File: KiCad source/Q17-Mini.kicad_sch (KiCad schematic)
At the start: 81 parts, among them J1 INPUT, J2-1 SPK+, J2-2 SPK-, J3-1 V+, J3-2 GND, J3-3 V-, Q1 IRF610, Q10 KSA992, Q11 BS250P, Q12 BD139, Q13 IRF610, Q14 IRF9610, Q15 FQA46N15, Q16 FQA36P15, Q2 KSA992, Q3 KSC1845, Q4 IRF9610, Q5 FQP3P20, Q6 FQP3N30, Q7 KSC1845, Q8 ZVN4206AV, Q9 BS250P, U1 OPA1641

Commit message: Update Q17-Mini.kicad_sch
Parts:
- removed H1: MountingHole, MountingHole:MountingHole_3.2mm_M3_Pad_Via, symbol Mechanical:MountingHole
- R23: value 10K -> 10k
- renumbered R30 to R30R
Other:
- note added: "Q8 : 2N7000 (not TA) or ZVN4206AV"
- note removed: "Q8 : 2N7000 (Not TA) or ZVN4206AV"

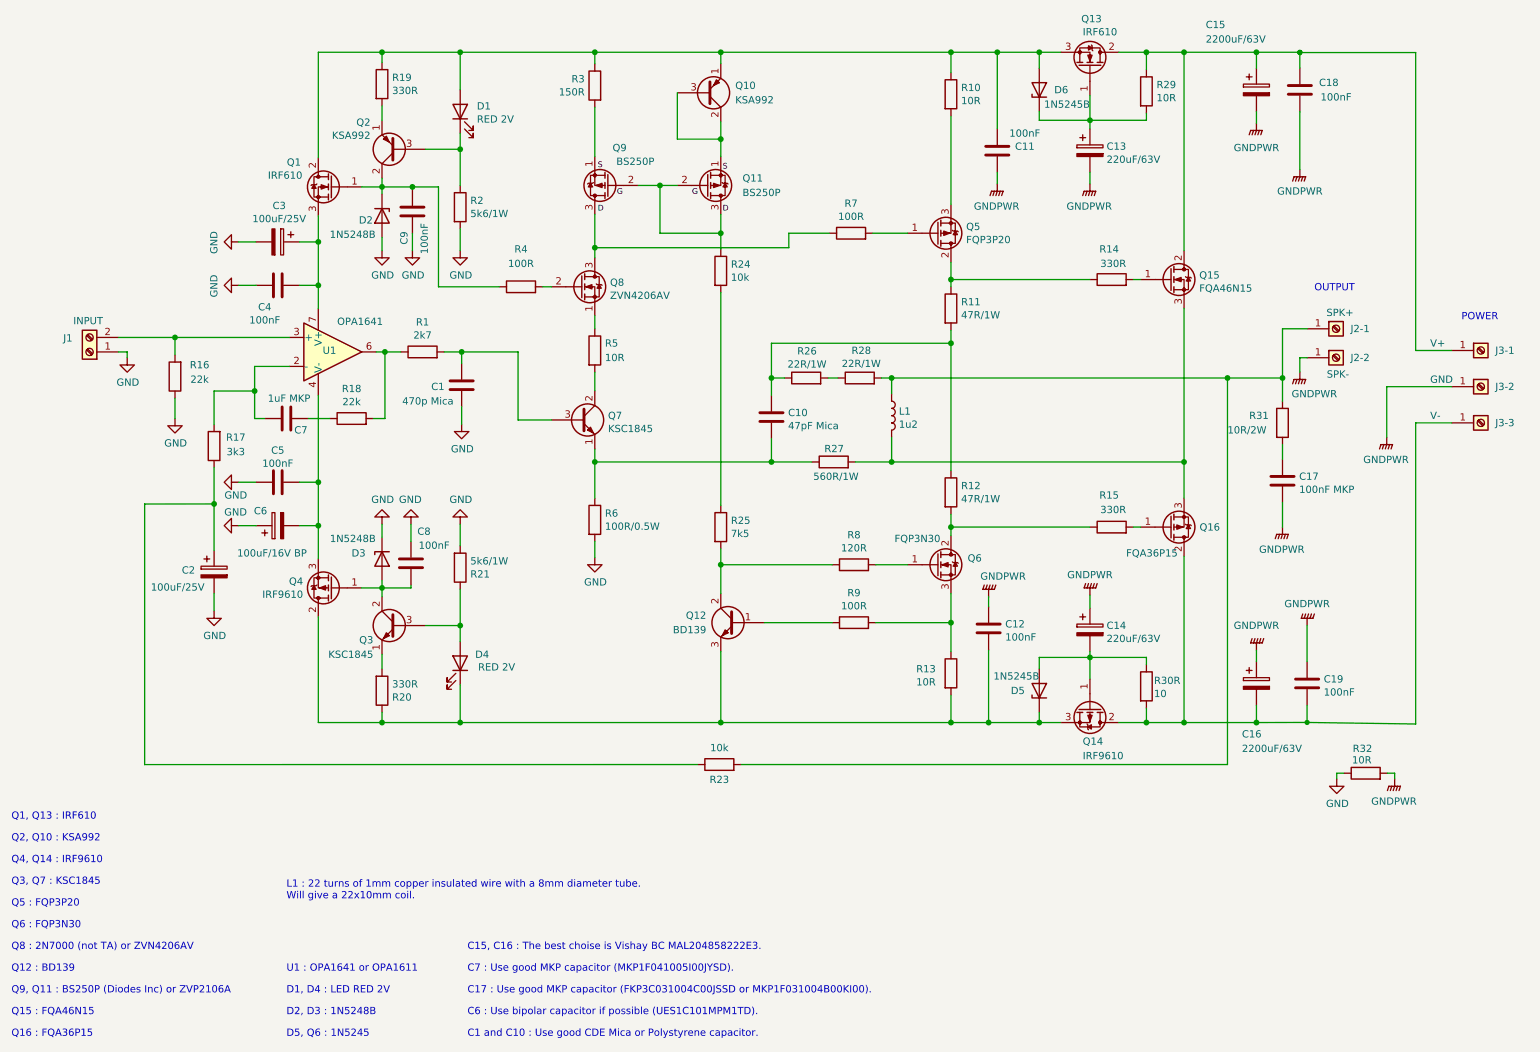
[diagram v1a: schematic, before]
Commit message: PCB v1.0.4
Works on components values and grounding.
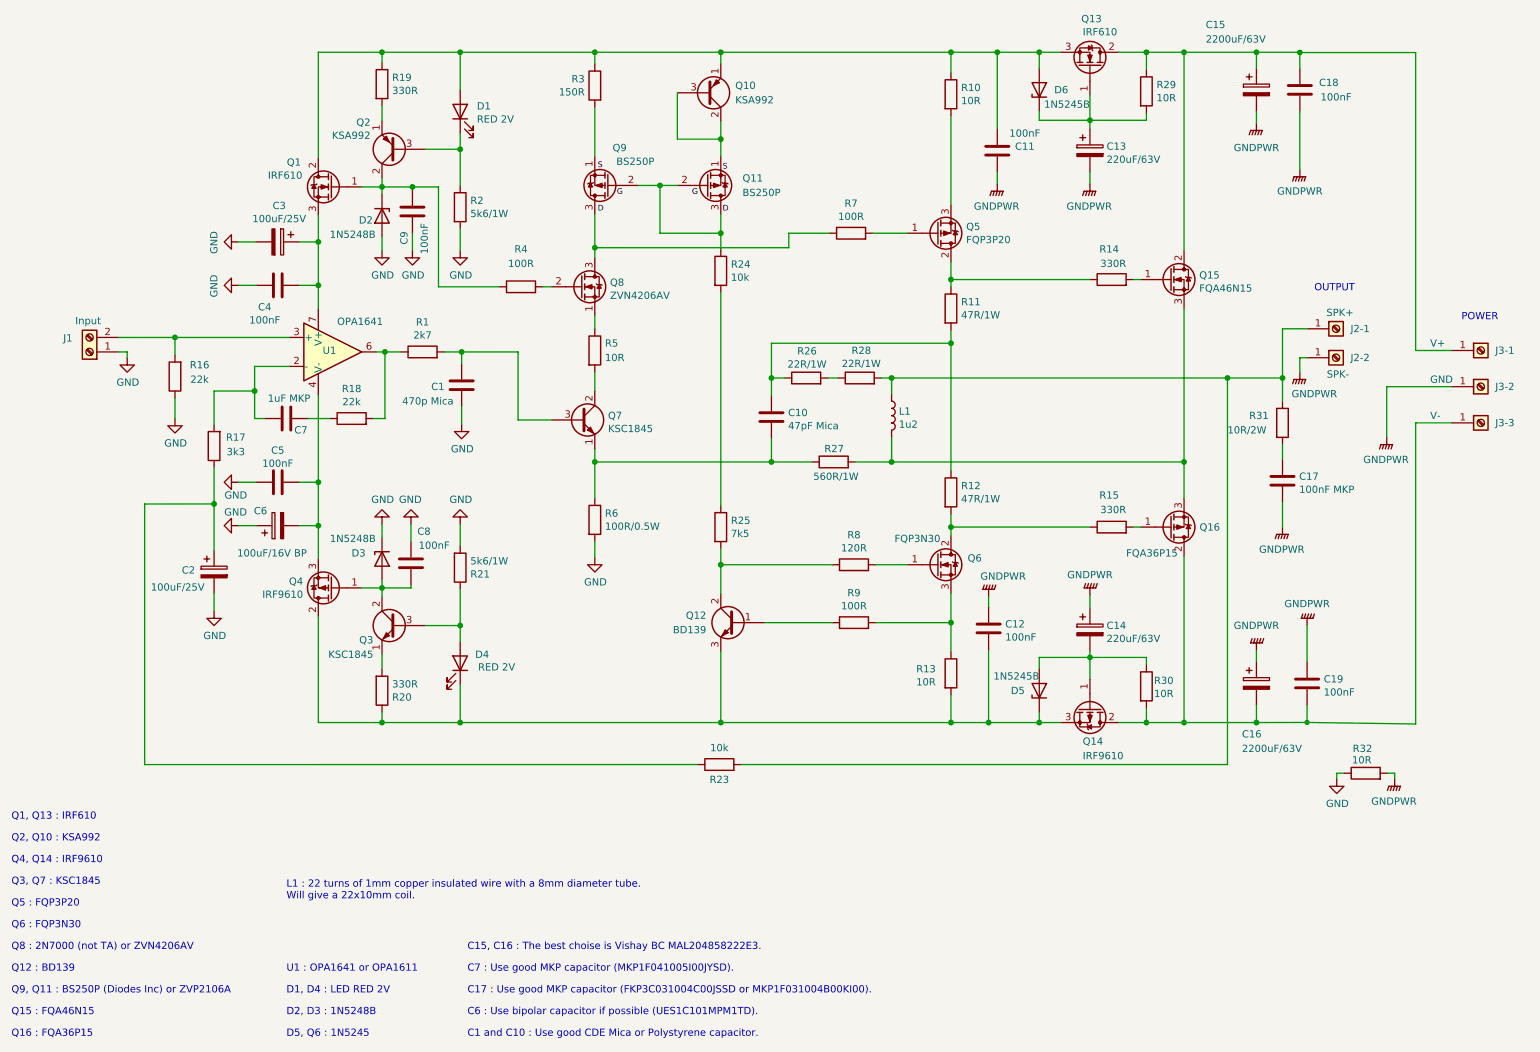
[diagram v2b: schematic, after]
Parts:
- C1, C10: footprint Capacitor_THT:C_Disc_D11.0mm_W5.0mm_P7.50mm -> Silver_Mica:C_Mica_L11.4mm_W4.3mm_H9.1_P5.9mm
- C11, C12, C18, C19, C4, C5, C8, C9: footprint Capacitor_THT:C_Disc_D7.5mm_W2.5mm_P5.00mm -> Capacitor_THT:C_Rect_L7.2mm_W2.5mm_P5.00mm_FKS2_FKP2_MKS2_MKP2
- C13, C14: footprint Capacitor_THT:CP_Radial_D10.0mm_P5.00mm_P7.50mm -> Capacitor_THT:CP_Radial_D12.5mm_P5.00mm
- C17: footprint Capacitor_THT:C_Rect_L18.0mm_W11.0mm_P15.00mm_FKS3_FKP3 -> Capacitor_THT:C_Rect_L18.0mm_W6.0mm_P15.00mm_FKS3_FKP3
- C2, C3, C6: footprint Capacitor_THT:C_Radial_D10.0mm_H12.5mm_P5.00mm -> Capacitor_THT:CP_Radial_D10.0mm_P5.00mm
- C7: footprint Capacitor_THT:CP_Axial_L26.5mm_D20.0mm_P33.00mm_Horizontal -> Capacitor_THT:C_Rect_C7_Q17-Mini
- J1: value INPUT -> Input; footprint Connector_Stocko:Stocko_MKS_1651-6-0-202_1x2_P2.50mm_Vertical -> TerminalBlock_Phoenix:TerminalBlock_Phoenix_PT-1,5-2-5.0-H_1x02_P5.00mm_Horizontal
- J2-1, J2-2, J3-1, J3-2, J3-3: footprint Connector_AMASS:AMASS_XT30U-F_1x02_P5.0mm_Vertical -> Connector_Faston:Faston_connector
- L1: footprint inductor:L -> Inductor_THT:L_Axial_L22mm_D10mm_P21mm_Horizontal_Q17_Mini
- Q10, Q2, Q3, Q7: footprint Package_TO_SOT_THT:TO-92 -> Package_TO_SOT_THT:TO-92_Inline_Wide
- Q11, Q9: footprint Package_TO_SOT_THT:TO-92_Inline -> Package_TO_SOT_THT:TO-92S
- Q15, Q16: footprint Package_TO_SOT_THT:TO-3P-3_Horizontal_TabDown -> Package_TO_SOT_THT:TO-3P-3_Vertical
- R30: renamed from R30R; value 10 -> 10R

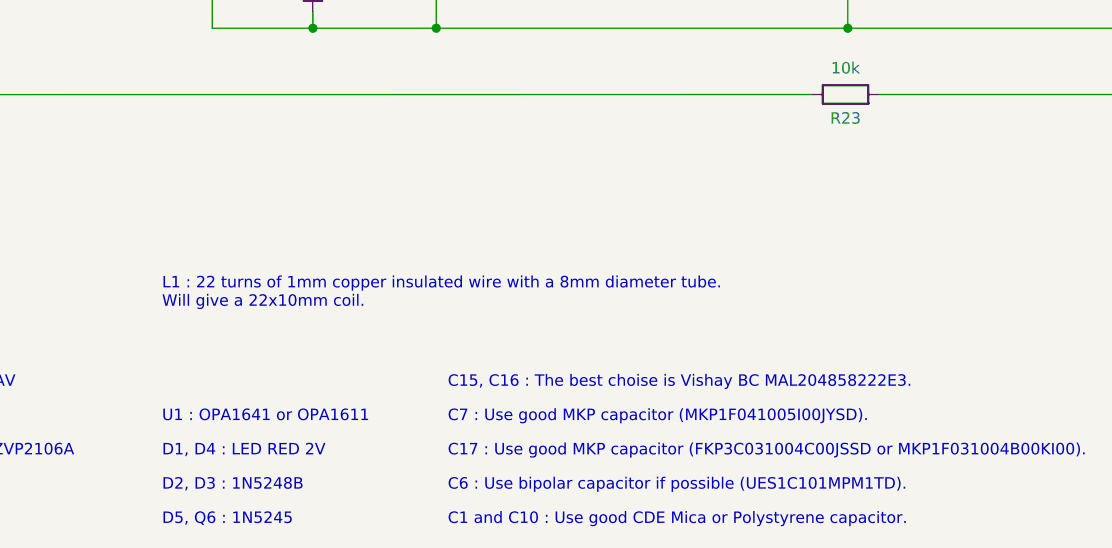
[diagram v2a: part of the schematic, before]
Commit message: Schematic v1.0.6
Changed specs of L1 coil.
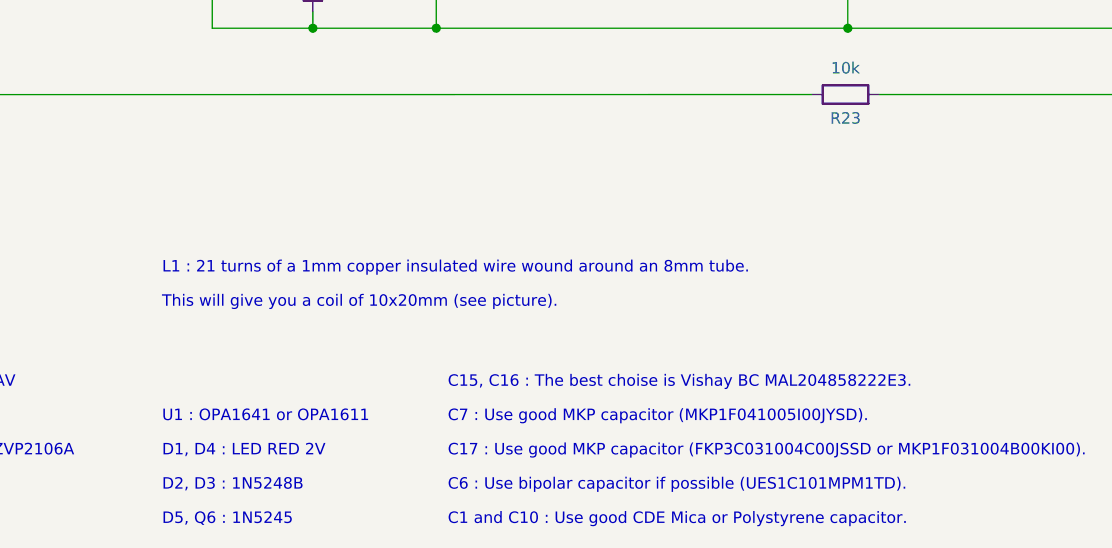
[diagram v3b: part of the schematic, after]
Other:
- note added: "L1 : 21 turns of a 1mm copper insulated wire wound around an 8mm tube."
- note added: "This will give you a coil of 10x20mm (see picture)."
- note removed: "L1 : 22 turns of 1mm copper insulated wire with a 8mm diameter tube. Will give a 22x10mm coil."

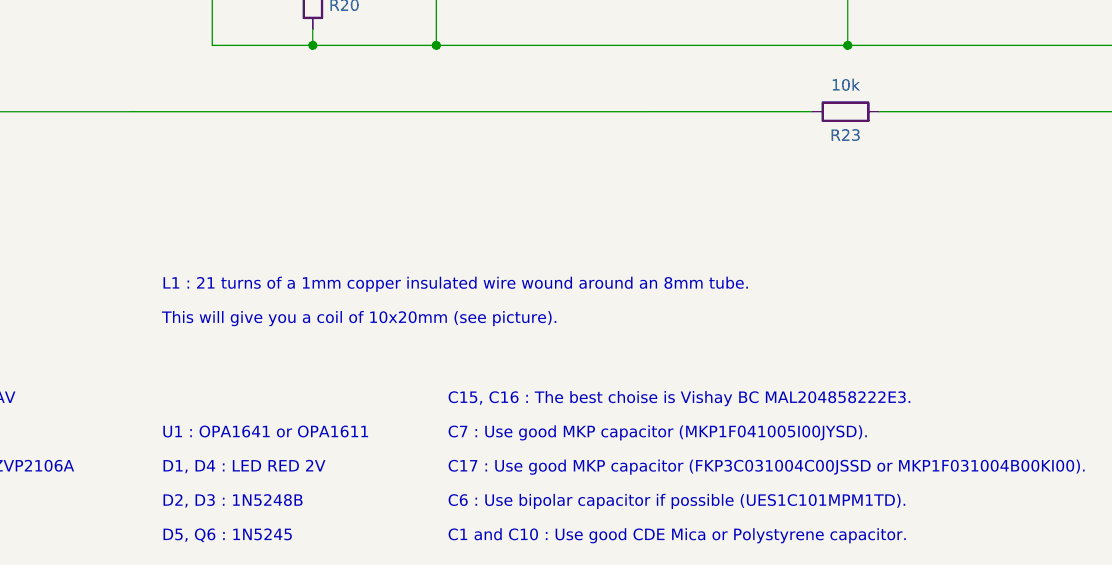
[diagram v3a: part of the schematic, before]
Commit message: PCB 1.0.5
- new PCB and Gerber files.
- new footprints for 1W and 2W resistors.
- resistor power wrote on the PCB.
- mods on schematic.
- new 3D files.
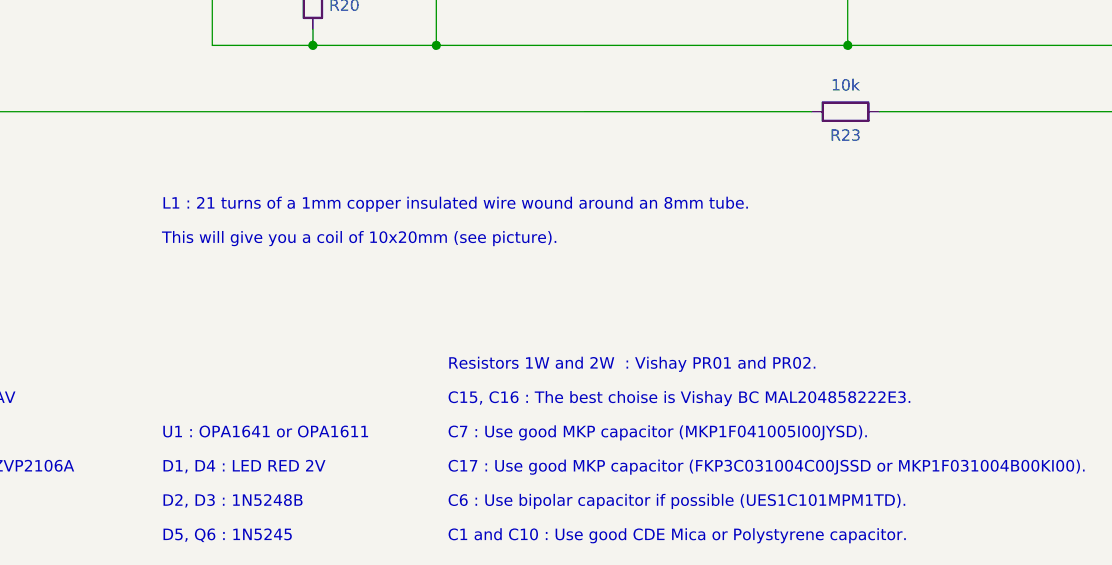
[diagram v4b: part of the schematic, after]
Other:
- note added: "Resistors 1W and 2W : Vishay PR01 and PR02."

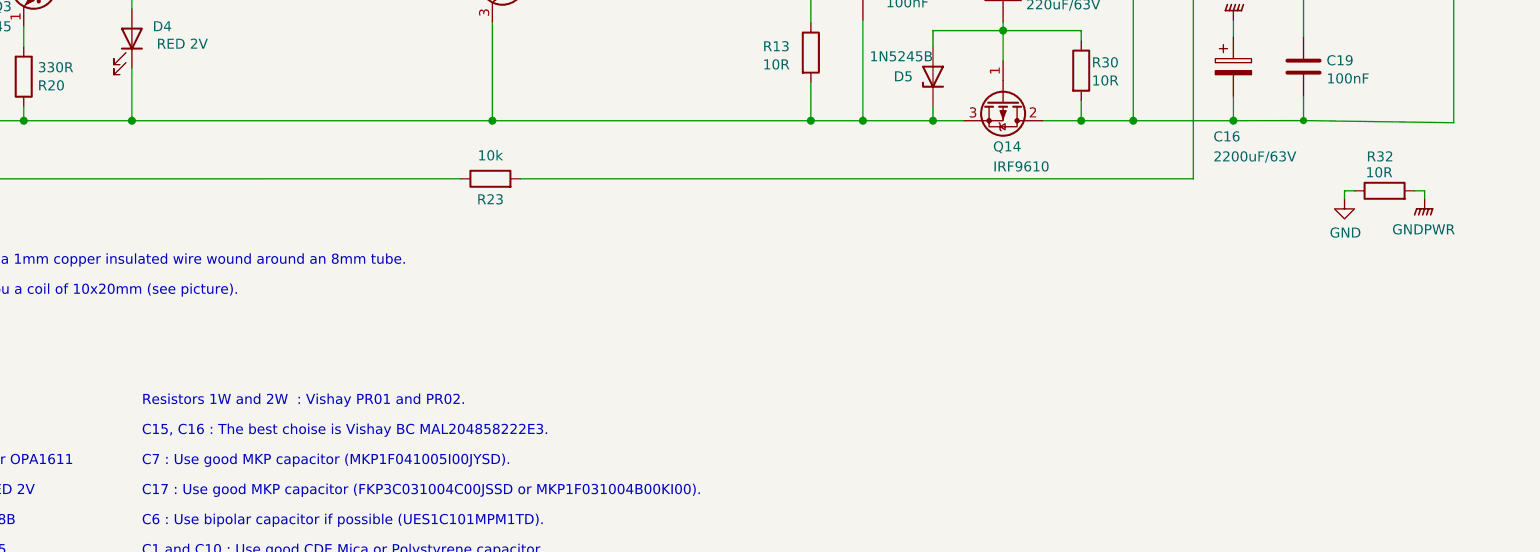
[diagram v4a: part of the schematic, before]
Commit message: PCB 1.0.6
- Moved R21 and R13. R21 was too far from D4.
- Moved some tracks.
- Schematic 1.0.7.
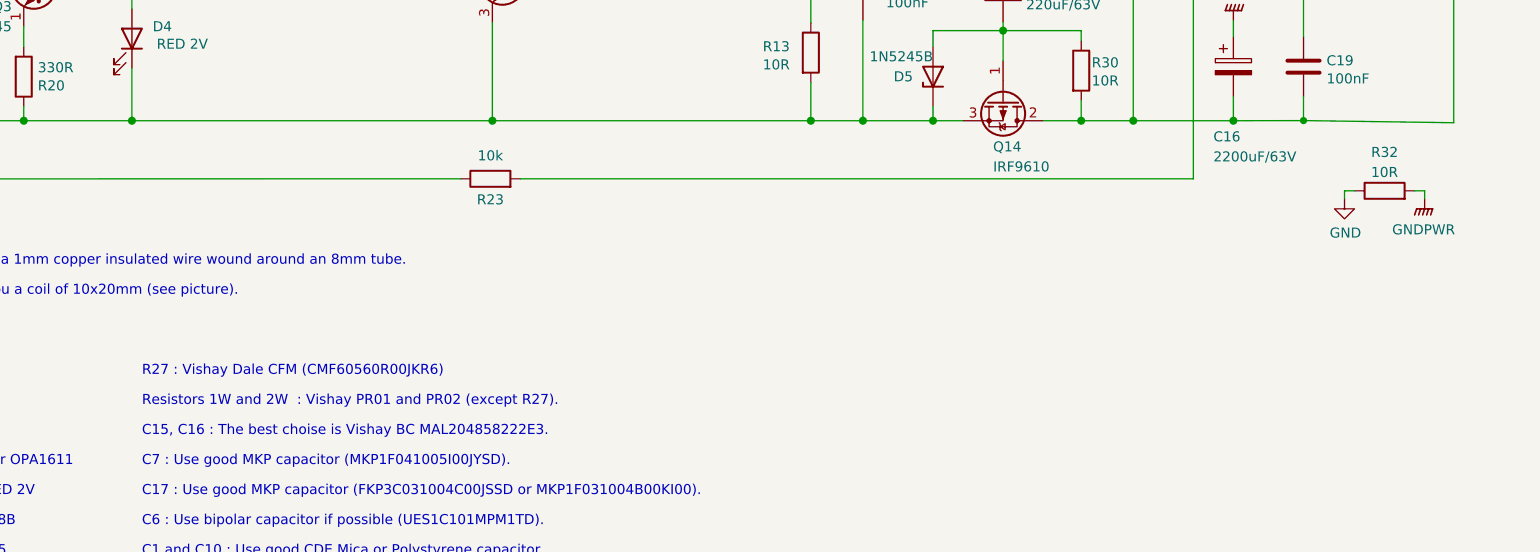
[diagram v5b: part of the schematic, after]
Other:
- note added: "R27 : Vishay Dale CFM (CMF60560R00JKR6)"
- note added: "Resistors 1W and 2W : Vishay PR01 and PR02 (except R27)."
- note removed: "Resistors 1W and 2W : Vishay PR01 and PR02."

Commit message: Schematic 1.0.7
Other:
- note added: "L1 : 22 turns of a 1mm copper insulated wire wound around an 8mm tube."
- note removed: "L1 : 21 turns of a 1mm copper insulated wire wound around an 8mm tube."

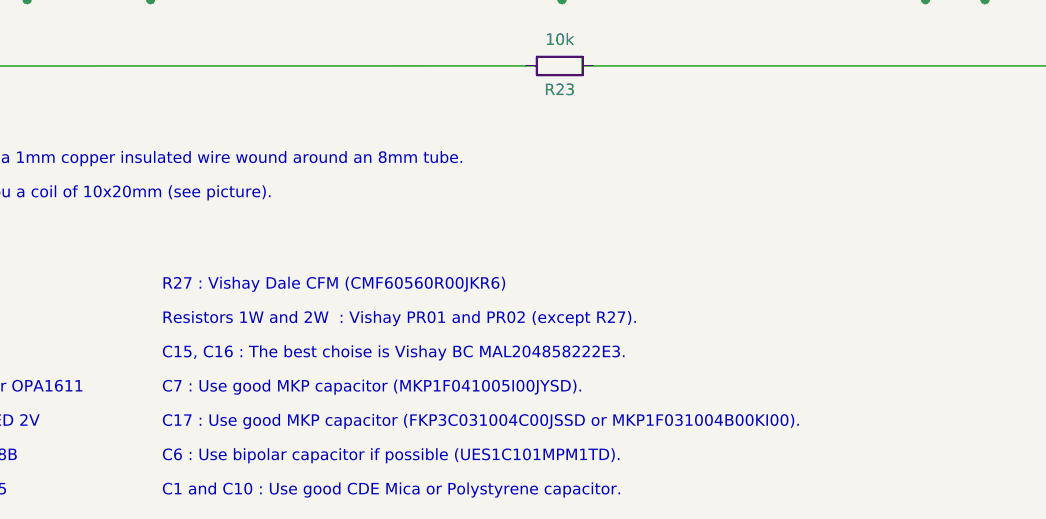
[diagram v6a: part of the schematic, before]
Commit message: Schematic 1.0.7
Number of turn for L1 change.
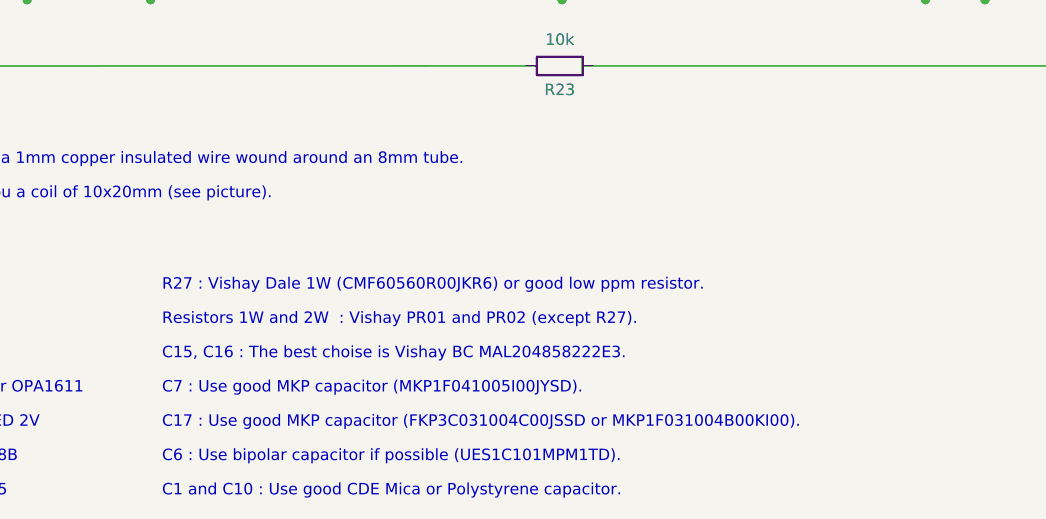
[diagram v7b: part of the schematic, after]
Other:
- note added: "R27 : Vishay Dale 1W (CMF60560R00JKR6) or good low ppm resistor."
- note removed: "R27 : Vishay Dale CFM (CMF60560R00JKR6)"
